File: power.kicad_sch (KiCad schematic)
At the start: 50 parts, among them J201 USBC, Q4 2N7002K, Q5 BSS83P, SW202 PWR_ON, U201 MAX17043G+T, U202 MCP73831-3-OT, U5 TPS630701RNMR

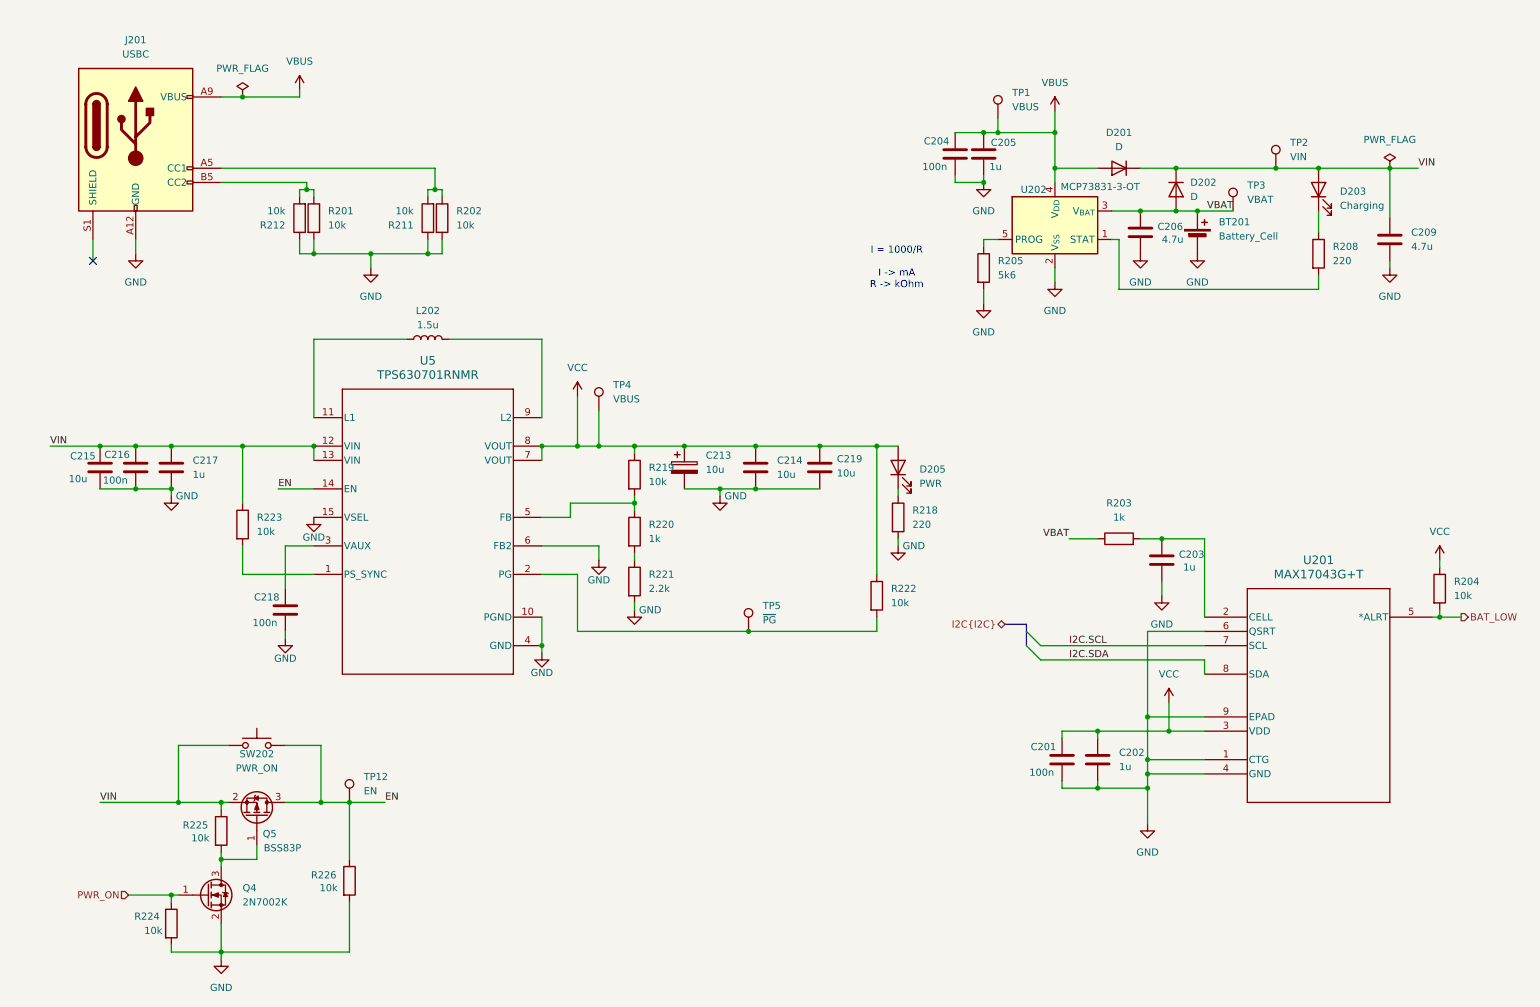
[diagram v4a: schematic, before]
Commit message: Assign component LCSC part numbers
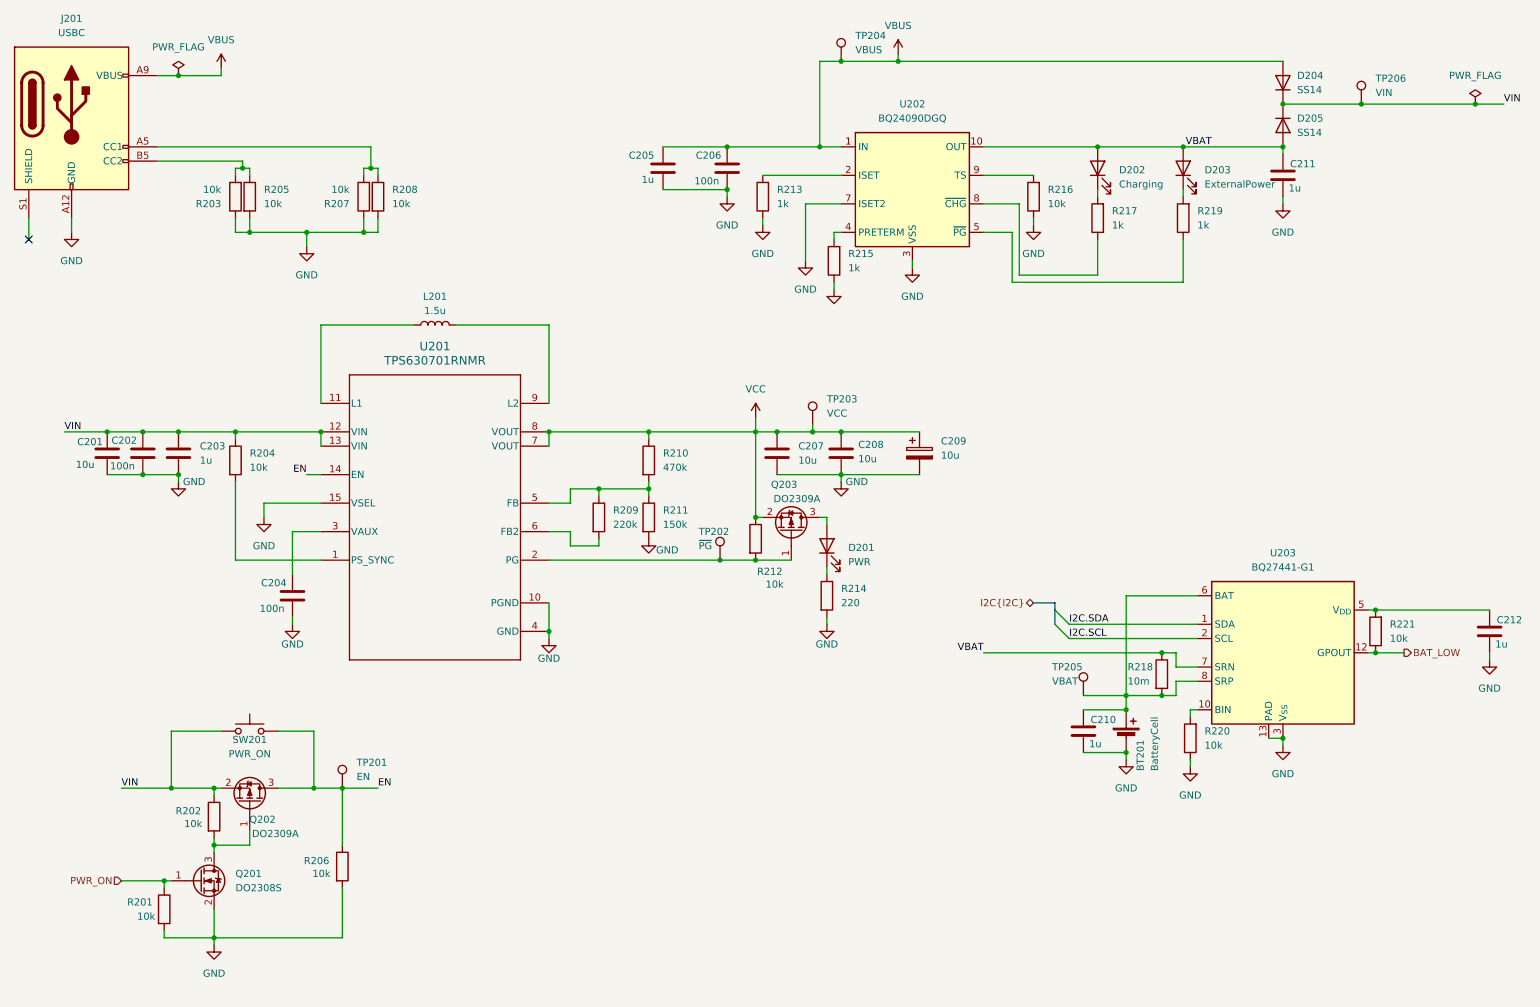
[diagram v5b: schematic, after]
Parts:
- removed C209: 4.7u, Capacitor_SMD:C_1206_3216Metric_Pad1.33x1.80mm_HandSolder, symbol Device:C
- removed C213: 10u, Capacitor_Tantalum_SMD:CP_EIA-7343-31_Kemet-D_HandSolder, symbol Device:C_Polarized
- removed C214, C215, C219: 10u, Capacitor_SMD:C_1206_3216Metric_Pad1.33x1.80mm_HandSolder, symbol Device:C
- removed C216, C218: 100n, Capacitor_SMD:C_1206_3216Metric_Pad1.33x1.80mm_HandSolder, symbol Device:C
- removed C217: 1u, Capacitor_SMD:C_1206_3216Metric_Pad1.33x1.80mm_HandSolder, symbol Device:C
- removed D201, D202: D, Diode_SMD:D_1206_3216Metric_Pad1.42x1.75mm_HandSolder, symbol Device:D
- removed D205: PWR, LED_SMD:LED_1206_3216Metric_Pad1.42x1.75mm_HandSolder, symbol Device:LED
- removed L202: 1.5u, Inductor_SMD_Wurth:L_Wurth_WE-LQSH-2512, symbol Device:L
- removed R201, R202, R222, R223: 10k, Resistor_SMD:R_1206_3216Metric_Pad1.30x1.75mm_HandSolder, symbol Device:R
- removed TP2: VIN, TestPoint:TestPoint_Pad_D1.0mm, symbol Connector:TestPoint
- removed TP4: VBUS, TestPoint:TestPoint_Pad_D1.0mm, symbol Connector:TestPoint
- removed TP5: ~{PG}, TestPoint:TestPoint_Pad_D1.0mm, symbol Connector:TestPoint
- removed U201: MAX17043G+T, lib:MAX17043, symbol MAX17043:MAX17043G+T
- removed U202: MCP73831-3-OT, Package_TO_SOT_SMD:SOT-23-5_HandSoldering, symbol Battery_Management:MCP73831-3-OT
- removed U5: TPS630701RNMR, lib:TPS63070, symbol TPS63070:TPS630701RNMR
- added C207, C208: 10u, Capacitor_SMD:C_1206_3216Metric_Pad1.33x1.80mm_HandSolder, symbol Device:C
- added C209: 10u, Capacitor_Tantalum_SMD:CP_EIA-7343-31_Kemet-D_HandSolder, symbol Device:C_Polarized
- added C210, C211, C212: 1u, Capacitor_SMD:C_0805_2012Metric_Pad1.18x1.45mm_HandSolder, symbol Device:C
- added D201: PWR, LED_SMD:LED_1206_3216Metric_Pad1.42x1.75mm_HandSolder, symbol Device:LED
- added D202: Charging, LED_SMD:LED_1206_3216Metric_Pad1.42x1.75mm_HandSolder, symbol Device:LED
- added D204, D205: SS14, Diode_SMD:D_SMA_Handsoldering, symbol Device:D
- added L201: 1.5u, Inductor_SMD:L_Cenker_CKCS4020, symbol Device:L
- added Q203: DO2309A, Package_TO_SOT_SMD:SOT-23_Handsoldering, symbol Transistor_FET:BSS83P
- added R207, R216: 10k, Resistor_SMD:R_1206_3216Metric_Pad1.30x1.75mm_HandSolder, symbol Device:R
- added R209: 220k, Resistor_SMD:R_0805_2012Metric_Pad1.20x1.40mm_HandSolder, symbol Device:R
- added R210: 470k, Resistor_SMD:R_0805_2012Metric_Pad1.20x1.40mm_HandSolder, symbol Device:R
- added R213, R215, R217: 1k, Resistor_SMD:R_1206_3216Metric_Pad1.30x1.75mm_HandSolder, symbol Device:R
- added R214: 220, Resistor_SMD:R_1206_3216Metric_Pad1.30x1.75mm_HandSolder, symbol Device:R
- added TP202: ~{PG}, TestPoint:TestPoint_Pad_D2.0mm, symbol Connector:TestPoint
- added TP203: VCC, TestPoint:TestPoint_Pad_D2.0mm, symbol Connector:TestPoint
- added TP206: VIN, TestPoint:TestPoint_Pad_D1.0mm, symbol Connector:TestPoint
- added U201: TPS630701RNMR, lib:TPS63070, symbol TPS63070:TPS630701RNMR
- added U202: BQ24090DGQ, Package_SO:HVSSOP-10-1EP_3x3mm_P0.5mm_EP1.57x1.88mm, symbol Battery_Management:BQ24090DGQ
- added U203: BQ27441-G1, Package_SON:Texas_S-PDSO-N12, symbol Battery_Management:BQ27441-G1
- BT201: value Battery_Cell -> BatteryCell; footprint Battery:BatteryHolder_MPD_BH-18650-PC2 -> Battery:BatteryHolder_MPD_BH-18650-PC; LCSC (none) -> C5290175
- C201: value 100n -> 10u; now left out of the parts list
- C202: value 1u -> 100n; now left out of the parts list
- C203, C205: footprint Capacitor_SMD:C_1206_3216Metric_Pad1.33x1.80mm_HandSolder -> Capacitor_SMD:C_0805_2012Metric_Pad1.18x1.45mm_HandSolder; LCSC (none) -> C7393927
- C204, R204, R212: now left out of the parts list
- C206: value 4.7u -> 100n; now left out of the parts list
- D203: value Charging -> ExternalPower; now left out of the parts list
- J201: LCSC (none) -> C42400234
- Q201: renamed from Q4; value 2N7002K -> DO2308S; footprint Package_TO_SOT_SMD:SOT-23 -> Package_TO_SOT_SMD:SOT-23_Handsoldering; LCSC (none) -> C47018572
- Q202: renamed from Q5; value BSS83P -> DO2309A; footprint Package_TO_SOT_SMD:SOT-23 -> Package_TO_SOT_SMD:SOT-23_Handsoldering; LCSC (none) -> C47018570
- R201: renamed from R224; now left out of the parts list
- R202: renamed from R225; now left out of the parts list
- R203, R220: value 1k -> 10k; now left out of the parts list
- R205: value 5k6 -> 10k; now left out of the parts list
- R206: renamed from R226; now left out of the parts list
- R208: value 220 -> 10k; now left out of the parts list
- R211: value 10k -> 150k; footprint Resistor_SMD:R_1206_3216Metric_Pad1.30x1.75mm_HandSolder -> Resistor_SMD:R_0805_2012Metric_Pad1.20x1.40mm_HandSolder; LCSC (none) -> C365243
- R218: value 220 -> 10m; footprint Resistor_SMD:R_1206_3216Metric_Pad1.30x1.75mm_HandSolder -> Resistor_SMD:R_0805_2012Metric_Pad1.20x1.40mm_HandSolder; LCSC (none) -> C2961480
- R219: value 10k -> 1k; now left out of the parts list
- R221: value 2.2k -> 10k; now left out of the parts list
- SW201: renamed from SW202; footprint Button_Switch_SMD:SW_SPST_PTS647_Sx38 -> Button_Switch_THT:SW_PUSH_6mm; now left out of the parts list
- TP201: renamed from TP12; footprint TestPoint:TestPoint_Pad_D1.0mm -> TestPoint:TestPoint_Pad_D2.0mm; now left out of the parts list
- TP205: renamed from TP3; footprint TestPoint:TestPoint_Pad_D1.0mm -> TestPoint:TestPoint_Pad_D2.0mm; now left out of the parts list
- renumbered TP1 to TP204
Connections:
- net BAT_LOW: now also R221.1, U203.12 (GPOUT); no longer R204.2
- net EN: now also U201.14 (EN)
- net GND: now also R203.1, R208.2, R211.2, R220.1, C207.2, C208.2, C209.2, C210.2, C211.2, C212.2, R207.1, R213.1, R214.2, R215.1, R216.1, U201.10 (PGND), U201.15 (VSEL), U201.4 (GND), U202.11 (VSS), U202.3 (VSS), U202.7 (ISET2), U203.13 (PAD), U203.3 (V_{SS}); no longer R211.1, R212.1, R218.2, R221.2
- net I2C.SCL: now also U203.2 (SCL)
- net I2C.SDA: now also U203.1 (SDA)
- net VBAT: now also D203.2 (A), R218.1, C211.1, D202.2 (A), D205.2 (A), U202.10 (OUT), U203.7 (SRN); no longer BT201.1 (+), C206.1, R203.1, TP205.1
- net VBUS: now also C206.1, D204.2 (A), U202.1 (IN); no longer C204.1
- net VCC: now also R212.1, C207.1, C208.1, C209.1, Q203.2 (S), R210.1, TP203.1, U201.7 (VOUT), U201.8 (VOUT); no longer C201.1, C202.1, R204.1, R219.1
- net VIN: now also C201.1, C202.1, C203.1, R204.1, D204.1 (K), D205.1 (K), TP206.1, U201.12 (VIN), U201.13 (VIN); no longer D203.2 (A)
- net at J201.B5 (CC2): now also R203.2, R205.1; no longer R212.2
- net at J201.A5 (CC1): now also R208.1, R207.2; no longer R211.2
- net at R219.2: now also D203.1 (K); no longer R220.1
- net at R220.2: now also U203.10 (BIN); no longer R221.1
- new net: R213.2, U202.2 (ISET)
- new net: R215.2, U202.4 (PRETERM)
- new net: R219.1, U202.5 (~{PG})
- new net: R217.1, U202.8 (~{CHG})
- new net: R216.2, U202.9 (TS)
- new net: BT201.1 (+), C210.1, R218.2, TP205.1, U203.6 (BAT), U203.8 (SRP)
- new net: Q203.1 (G), R212.2, TP202.1, U201.2 (PG)
- new net: R204.2, U201.1 (PS_SYNC)
- new net: L201.1, U201.11 (L1)
- new net: C204.1, U201.3 (VAUX)
- new net: R209.1, R210.2, R211.1, U201.5 (FB)
- new net: R209.2, U201.6 (FB2)
- new net: L201.2, U201.9 (L2)
- new net: C212.1, R221.2, U203.5 (V_{DD})
- new net: D201.2 (A), Q203.3 (D)
- new net: D201.1 (K), R214.1
- new net: D202.1 (K), R217.2
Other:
- note removed: "I = 1000/R I -> mA R -> kOhm"
- moved on the sheet: BT201, J201, Q201, Q202, R201, R202, R206, SW201, TP201, TP204, TP205

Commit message: Simplify some schematics to reduce BOM
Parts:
- TP201, TP202, TP203, TP205: footprint TestPoint:TestPoint_Pad_D2.0mm -> TestPoint:TestPoint_Pad_D1.0mm
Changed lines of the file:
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@@
 			)
 		)
-		(property "Footprint" "TestPoint:TestPoint_Pad_D2.0mm"
+		(property "Footprint" "TestPoint:TestPoint_Pad_D1.0mm"
 			(at 77.47 152.4 0)
 			(effects
@@
 			)
 		)
-		(property "Footprint" "TestPoint:TestPoint_Pad_D2.0mm"
+		(property "Footprint" "TestPoint:TestPoint_Pad_D1.0mm"
 			(at 209.55 135.89 0)
 			(effects
@@
 			)
 		)
-		(property "Footprint" "TestPoint:TestPoint_Pad_D2.0mm"
+		(property "Footprint" "TestPoint:TestPoint_Pad_D1.0mm"
 			(at 161.29 87.63 0)
 			(effects
@@
 			)
 		)
-		(property "Footprint" "TestPoint:TestPoint_Pad_D2.0mm"
+		(property "Footprint" "TestPoint:TestPoint_Pad_D1.0mm"
 			(at 144.78 111.76 0)
 			(effects

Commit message: Update BOM options for export
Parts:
- TP204, TP206: now left out of the parts list
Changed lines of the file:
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@@
 		(unit 1)
 		(exclude_from_sim no)
-		(in_bom yes)
+		(in_bom no)
 		(on_board yes)
 		(dnp no)
@@
 		(unit 1)
 		(exclude_from_sim no)
-		(in_bom yes)
-		(on_board yes)
-		(dnp no)
+		(in_bom no)
+		(on_board yes)
+		(dnp no)
